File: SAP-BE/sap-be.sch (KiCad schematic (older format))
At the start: 0 parts

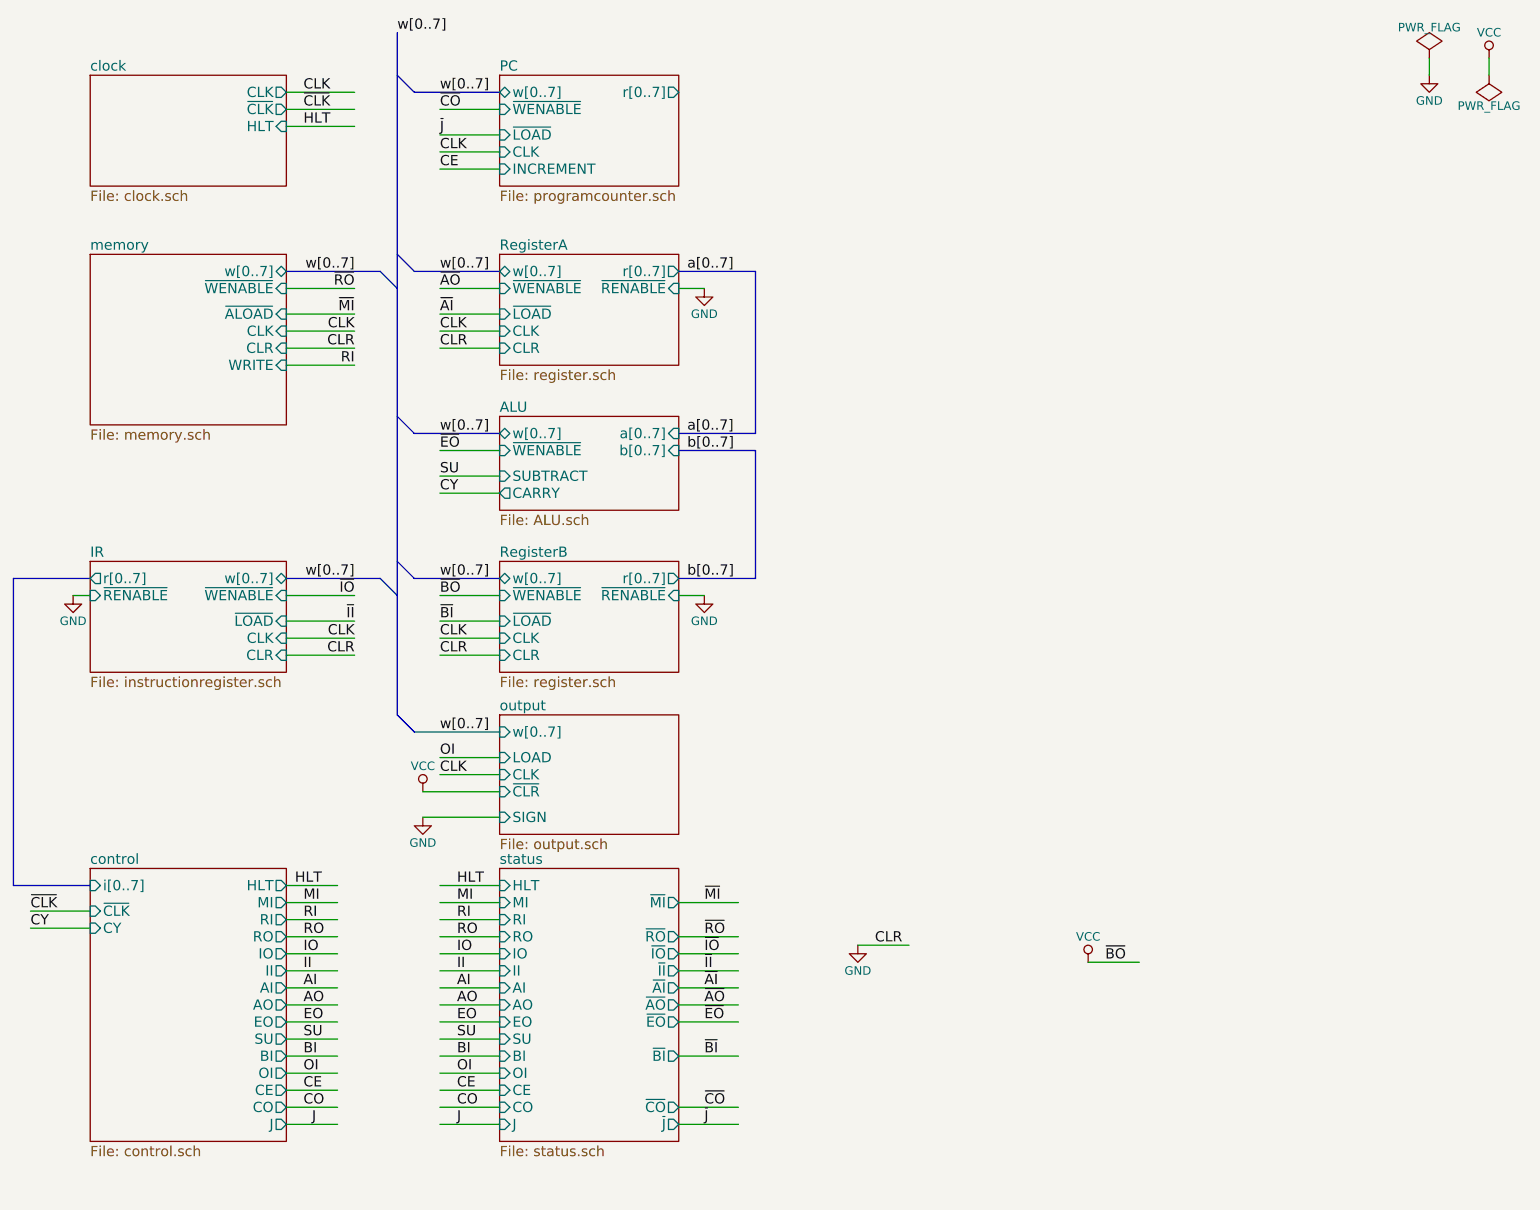
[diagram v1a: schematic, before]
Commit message: Update with changes for reset
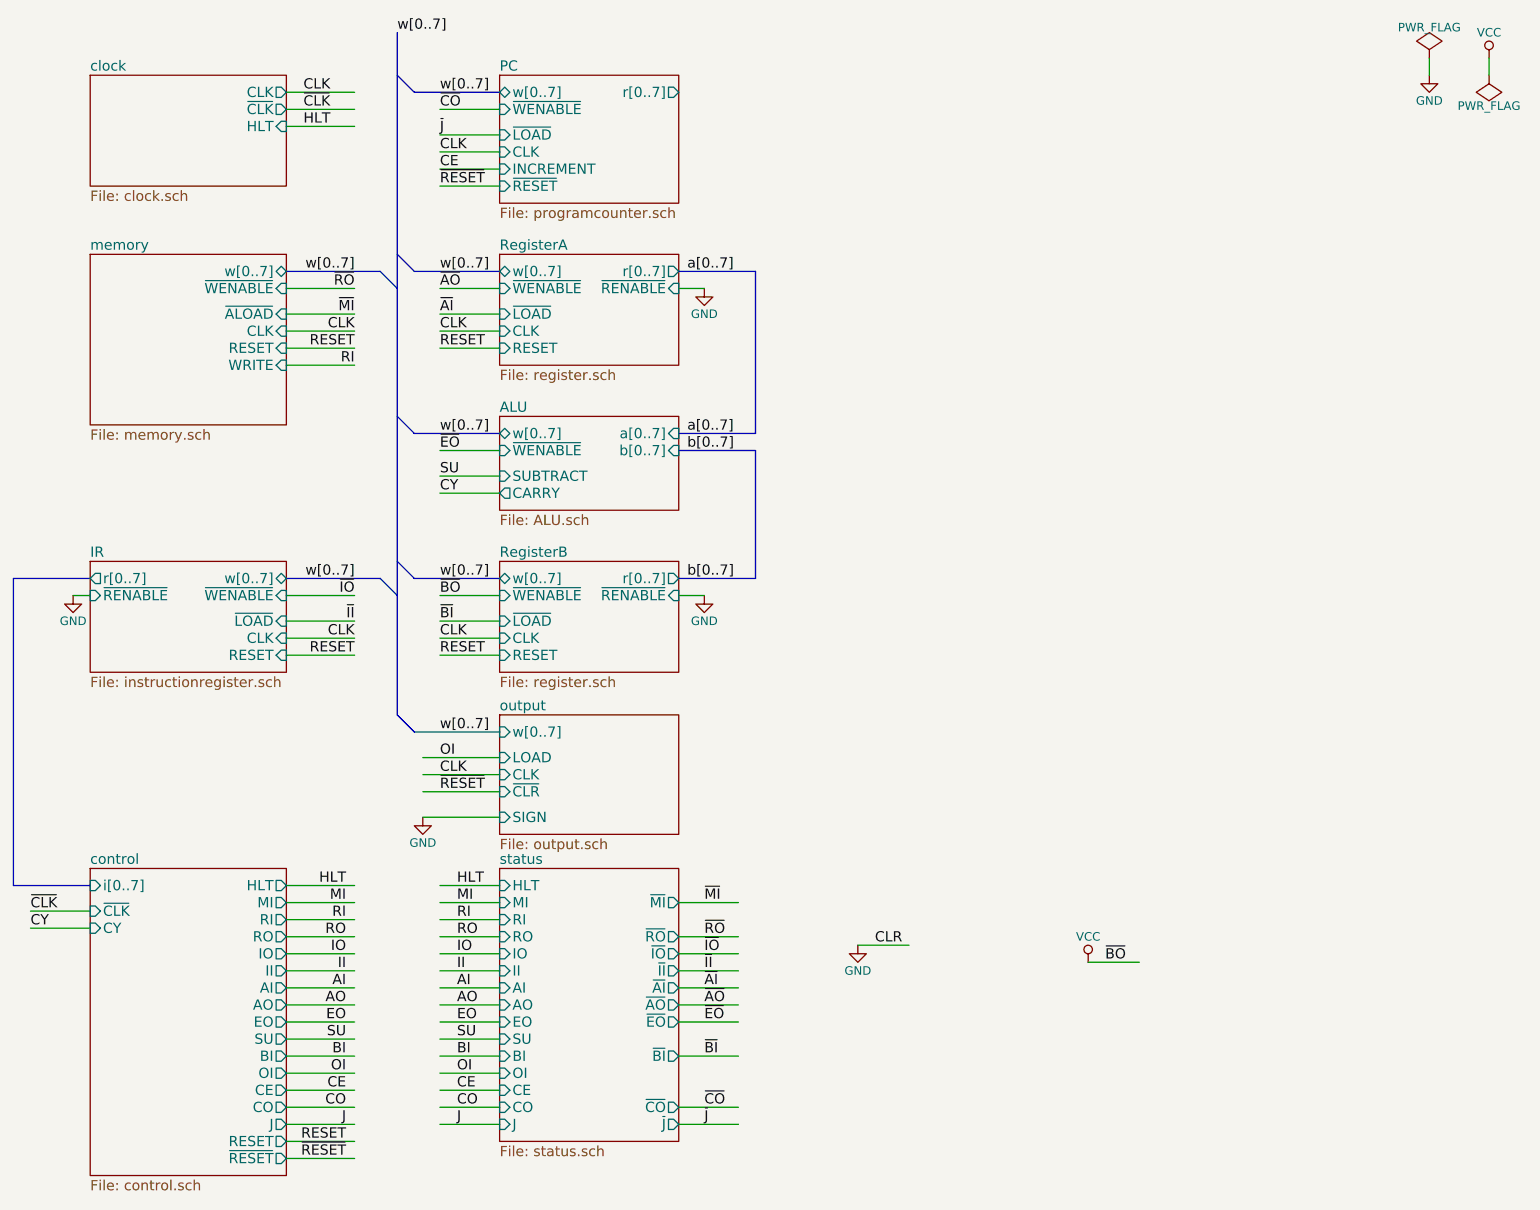
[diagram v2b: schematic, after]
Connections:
- net labels added: RESET, ~RESET
- wire segments 80 -> 83
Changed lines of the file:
@@
 $EndSheet
 $Comp
-L GND #PWR6
+L GND #PWR01
 U 1 1 59143FF4
 P 7200 6050
-F 0 "#PWR6" H 7200 5800 50  0001 C CNN
+F 0 "#PWR01" H 7200 5800 50  0001 C CNN
 F 1 "GND" H 7200 5900 50  0000 C CNN
 F 2 "" H 7200 6050 50  0000 C CNN
@@
 Text Label 4750 3150 0    60   ~ 0
 ~EO
-Text Label 4750 4350 0    60   ~ 0
-CLR
-Text Label 4750 2550 0    60   ~ 0
-CLR
 $Sheet
 S 2700 950  1150 650
@@
 $EndSheet
 $Comp
-L PWR_FLAG #FLG1
+L PWR_FLAG #FLG02
 U 1 1 590D3658
 P 10550 850
-F 0 "#FLG1" H 10550 945 50  0001 C CNN
+F 0 "#FLG02" H 10550 945 50  0001 C CNN
 F 1 "PWR_FLAG" H 10550 1030 50  0000 C CNN
 F 2 "" H 10550 850 50  0000 C CNN
@@
 $EndComp
 $Comp
-L PWR_FLAG #FLG2
+L PWR_FLAG #FLG03
 U 1 1 590D37F8
 P 10900 950
-F 0 "#FLG2" H 10900 1045 50  0001 C CNN
+F 0 "#FLG03" H 10900 1045 50  0001 C CNN
 F 1 "PWR_FLAG" H 10900 1130 50  0000 C CNN
 F 2 "" H 10900 950 50  0000 C CNN
@@
 $EndComp
 $Comp
-L GND #PWR8
+L GND #PWR04
 U 1 1 590D3998
 P 10550 950
-F 0 "#PWR8" H 10550 700 50  0001 C CNN
+F 0 "#PWR04" H 10550 700 50  0001 C CNN
 F 1 "GND" H 10550 800 50  0000 C CNN
 F 2 "" H 10550 950 50  0000 C CNN
@@
 $EndComp
 $Comp
-L VCC #PWR9
+L VCC #PWR05
 U 1 1 590D3B38
 P 10900 850
-F 0 "#PWR9" H 10900 700 50  0001 C CNN
+F 0 "#PWR05" H 10900 700 50  0001 C CNN
 F 1 "VCC" H 10900 1000 50  0000 C CNN
 F 2 "" H 10900 850 50  0000 C CNN
@@
 F1 "register.sch" 60
 F2 "~RENABLE" I R 6150 4000 60
-F3 "CLR" I L 5100 4350 60
-F4 "~LOAD" I L 5100 4150 60
-F5 "~WENABLE" I L 5100 4000 60
-F6 "w[0..7]" B L 5100 3900 60
-F7 "CLK" I L 5100 4250 60
-F8 "r[0..7]" O R 6150 3900 60
+F3 "~LOAD" I L 5100 4150 60
+F4 "~WENABLE" I L 5100 4000 60
+F5 "w[0..7]" B L 5100 3900 60
+F6 "CLK" I L 5100 4250 60
+F7 "r[0..7]" O R 6150 3900 60
+F8 "RESET" I L 5100 4350 60
 $EndSheet
 $Sheet
@@
 F1 "register.sch" 60
 F2 "~RENABLE" I R 6150 2200 60
-F3 "CLR" I L 5100 2550 60
-F4 "~LOAD" I L 5100 2350 60
-F5 "w[0..7]" B L 5100 2100 60
-F6 "~WENABLE" I L 5100 2200 60
-F7 "CLK" I L 5100 2450 60
-F8 "r[0..7]" O R 6150 2100 60
-$EndSheet
-$Comp
-L GND #PWR5
+F3 "~LOAD" I L 5100 2350 60
+F4 "w[0..7]" B L 5100 2100 60
+F5 "~WENABLE" I L 5100 2200 60
+F6 "CLK" I L 5100 2450 60
+F7 "r[0..7]" O R 6150 2100 60
+F8 "RESET" I L 5100 2550 60
+$EndSheet
+$Comp
+L GND #PWR06
 U 1 1 591162DB
 P 6300 4000
-F 0 "#PWR5" H 6300 3750 50  0001 C CNN
+F 0 "#PWR06" H 6300 3750 50  0001 C CNN
 F 1 "GND" H 6300 3850 50  0000 C CNN
 F 2 "" H 6300 4000 50  0000 C CNN
@@
 Text Label 7300 6050 0    60   ~ 0
 CLR
-Text Label 3950 6600 0    60   ~ 0
+Text Label 4200 6600 2    60   ~ 0
 SU
 Text Label 6300 6500 0    60   ~ 0
@@
 a[0..7]
 $Comp
-L GND #PWR4
+L GND #PWR07
 U 1 1 5915EFD4
 P 6300 2200
-F 0 "#PWR4" H 6300 1950 50  0001 C CNN
+F 0 "#PWR07" H 6300 1950 50  0001 C CNN
 F 1 "GND" H 6300 2050 50  0000 C CNN
 F 2 "" H 6300 2200 50  0000 C CNN
@@
 b[0..7]
 $Sheet
-S 5100 950  1050 650
+S 5100 950  1050 750
 U 5918B711
 F0 "PC" 60
@@
 F6 "CLK" I L 5100 1400 60
 F7 "r[0..7]" O R 6150 1050 60
+F8 "~RESET" I L 5100 1600 60
 $EndSheet
 Entry Bus Bus
@@
 Text Label 6300 7100 0    60   ~ 0
 ~J
-Text Label 3950 6900 0    60   ~ 0
+Text Label 4200 6900 2    60   ~ 0
 CE
 Text Label 4750 3400 0    60   ~ 0
@@
 F3 "CLK" I R 3850 2450 60
 F4 "~ALOAD" I R 3850 2350 60
-F5 "CLR" I R 3850 2550 60
-F6 "~WENABLE" I R 3850 2200 60
-F7 "WRITE" I R 3850 2650 60
-$EndSheet
-$Sheet
-S 2700 5600 1150 1600
+F5 "~WENABLE" I R 3850 2200 60
+F6 "WRITE" I R 3850 2650 60
+F7 "RESET" I R 3850 2550 60
+$EndSheet
+$Sheet
+S 2700 5600 1150 1800
 U 591ACE0B
 F0 "control" 60
@@
 F18 "CO" O R 3850 7000 60
 F19 "J" O R 3850 7100 60
+F20 "RESET" O R 3850 7200 60
+F21 "~RESET" O R 3850 7300 60
 $EndSheet
 Wire Wire Line
@@
 F1 "instructionregister.sch" 60
 F2 "~RENABLE" I L 2700 4000 60
-F3 "CLR" I R 3850 4350 60
-F4 "~LOAD" I R 3850 4150 60
-F5 "~WENABLE" I R 3850 4000 60
-F6 "w[0..7]" T R 3850 3900 60
-F7 "CLK" I R 3850 4250 60
-F8 "r[0..7]" O L 2700 3900 60
+F3 "~LOAD" I R 3850 4150 60
+F4 "~WENABLE" I R 3850 4000 60
+F5 "w[0..7]" T R 3850 3900 60
+F6 "CLK" I R 3850 4250 60
+F7 "r[0..7]" O L 2700 3900 60
+F8 "RESET" I R 3850 4350 60
 $EndSheet
 Entry Bus Bus
@@
 Text Label 4250 4250 2    60   ~ 0
 CLK
-Text Label 4250 4350 2    60   ~ 0
-CLR
 Wire Wire Line
 	4250 4000 3850 4000
@@
 ~II
 $Comp
-L GND #PWR1
+L GND #PWR08
 U 1 1 5914424C
 P 2600 4000
-F 0 "#PWR1" H 2600 3750 50  0001 C CNN
+F 0 "#PWR08" H 2600 3750 50  0001 C CNN
 F 1 "GND" H 2600 3850 50  0000 C CNN
 F 2 "" H 2600 4000 50  0000 C CNN
@@
 	2700 4000 2600 4000
 Wire Wire Line
-	5100 4950 4750 4950
-Wire Wire Line
-	5100 5050 4750 5050
+	4650 4950 5100 4950
+Wire Wire Line
+	4650 5050 5100 5050
 Wire Wire Line
 	4650 5150 5100 5150
@@
 CLK
 $Comp
-L VCC #PWR2
-U 1 1 5912653E
-P 4650 5150
-F 0 "#PWR2" H 4650 5000 50  0001 C CNN
-F 1 "VCC" H 4650 5300 50  0000 C CNN
-F 2 "" H 4650 5150 50  0000 C CNN
-F 3 "" H 4650 5150 50  0000 C CNN
-	1    4650 5150
-	1    0    0    -1
-$EndComp
-$Comp
-L GND #PWR3
+L GND #PWR09
 U 1 1 591266F0
 P 4650 5300
-F 0 "#PWR3" H 4650 5050 50  0001 C CNN
+F 0 "#PWR09" H 4650 5050 50  0001 C CNN
 F 1 "GND" H 4650 5150 50  0000 C CNN
 F 2 "" H 4650 5300 50  0000 C CNN
@@
 ~IO
 $Comp
-L VCC #PWR7
+L VCC #PWR010
 U 1 1 591A255E
 P 8550 6150
-F 0 "#PWR7" H 8550 6000 50  0001 C CNN
+F 0 "#PWR010" H 8550 6000 50  0001 C CNN
 F 1 "VCC" H 8550 6300 50  0000 C CNN
 F 2 "" H 8550 6150 50  0000 C CNN
@@
 ~CLK
 Wire Wire Line
-	4150 5700 3850 5700
-Wire Wire Line
-	4150 5800 3850 5800
-Wire Wire Line
-	4150 5900 3850 5900
-Wire Wire Line
-	4150 6000 3850 6000
-Wire Wire Line
-	4150 6100 3850 6100
-Wire Wire Line
-	4150 6200 3850 6200
-Wire Wire Line
-	4150 6300 3850 6300
-Wire Wire Line
-	4150 6400 3850 6400
-Wire Wire Line
-	3850 6500 4150 6500
-Wire Wire Line
-	4150 6600 3850 6600
-Wire Wire Line
-	4150 6700 3850 6700
-Wire Wire Line
-	4150 6800 3850 6800
-Wire Wire Line
-	4150 6900 3850 6900
-Wire Wire Line
-	4150 7000 3850 7000
-Wire Wire Line
-	4150 7100 3850 7100
+	3850 5700 4250 5700
+Wire Wire Line
+	3850 5800 4250 5800
+Wire Wire Line
+	3850 5900 4250 5900
+Wire Wire Line
+	3850 6000 4250 6000
+Wire Wire Line
+	3850 6100 4250 6100
+Wire Wire Line
+	3850 6200 4250 6200
+Wire Wire Line
+	3850 6300 4250 6300
+Wire Wire Line
+	3850 6400 4250 6400
+Wire Wire Line
+	3850 6500 4250 6500
+Wire Wire Line
+	3850 6600 4250 6600
+Wire Wire Line
+	3850 6700 4250 6700
+Wire Wire Line
+	3850 6800 4250 6800
+Wire Wire Line
+	3850 6900 4250 6900
+Wire Wire Line
+	3850 7000 4250 7000
+Wire Wire Line
+	3850 7100 4250 7100
 Wire Wire Line
 	4750 5700 5100 5700
@@
 Text Label 4850 6900 0    60   ~ 0
 CE
-Text Label 4000 7100 0    60   ~ 0
+Text Label 4200 7100 2    60   ~ 0
 J
 Text Label 4850 7100 0    60   ~ 0
 J
-Text Label 3950 7000 0    60   ~ 0
+Text Label 4200 7000 2    60   ~ 0
 CO
 Text Label 4850 7000 0    60   ~ 0
 CO
-Text Label 3900 5700 0    60   ~ 0
+Text Label 4200 5700 2    60   ~ 0
 HLT
 Text Label 4850 5700 0    60   ~ 0
 HLT
-Text Label 3950 5800 0    60   ~ 0
+Text Label 4200 5800 2    60   ~ 0
 MI
-Text Label 3950 5900 0    60   ~ 0
+Text Label 4200 5900 2    60   ~ 0
 RI
-Text Label 3950 6000 0    60   ~ 0
+Text Label 4200 6000 2    60   ~ 0
 RO
-Text Label 3950 6100 0    60   ~ 0
+Text Label 4200 6100 2    60   ~ 0
 IO
-Text Label 3950 6200 0    60   ~ 0
+Text Label 4200 6200 2    60   ~ 0
 II
-Text Label 3950 6300 0    60   ~ 0
+Text Label 4200 6300 2    60   ~ 0
 AI
-Text Label 3950 6400 0    60   ~ 0
+Text Label 4200 6400 2    60   ~ 0
 AO
-Text Label 3950 6500 0    60   ~ 0
+Text Label 4200 6500 2    60   ~ 0
 EO
-Text Label 3950 6700 0    60   ~ 0
+Text Label 4200 6700 2    60   ~ 0
 BI
-Text Label 3950 6800 0    60   ~ 0
+Text Label 4200 6800 2    60   ~ 0
 OI
 Text Label 4850 5800 0    60   ~ 0
@@
 Text Label 4250 2450 2    60   ~ 0
 CLK
-Text Label 4250 2550 2    60   ~ 0
-CLR
 Text Label 4250 2650 2    60   ~ 0
 RI
@@
 Text Label 4250 2100 2    60   ~ 0
 w[0..7]
+Wire Wire Line
+	5100 1600 4750 1600
+Text Label 4750 1600 0    60   ~ 0
+~RESET
+Text Label 4750 2550 0    60   ~ 0
+RESET
+Text Label 4750 4350 0    60   ~ 0
+RESET
+Text Label 4250 4350 2    60   ~ 0
+RESET
+Text Label 4250 2550 2    60   ~ 0
+RESET
+Text Label 4750 5150 0    60   ~ 0
+~RESET
+Wire Wire Line
+	3850 7200 4250 7200
+Wire Wire Line
+	3850 7300 4250 7300
+Text Label 4200 7200 2    60   ~ 0
+RESET
+Text Label 4200 7300 2    60   ~ 0
+~RESET
 $EndSCHEMATC

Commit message: Update with conditional flags
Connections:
- net labels added: CF, CRY, FI, ZF, ZRO, ~FI
- net labels removed: CY
- wire segments 83 -> 95
